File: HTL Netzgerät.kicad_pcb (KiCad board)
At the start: 2 copper layers, 140 x 65 mm, 57 parts, among them J1 0.7/20.32mm, T1 BC547, T2 BC547, T3 BC547, T4 BC547, T5 BC547, T6 BC557, T7 BC557, T8 BC639, X1 AUX1_AC1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

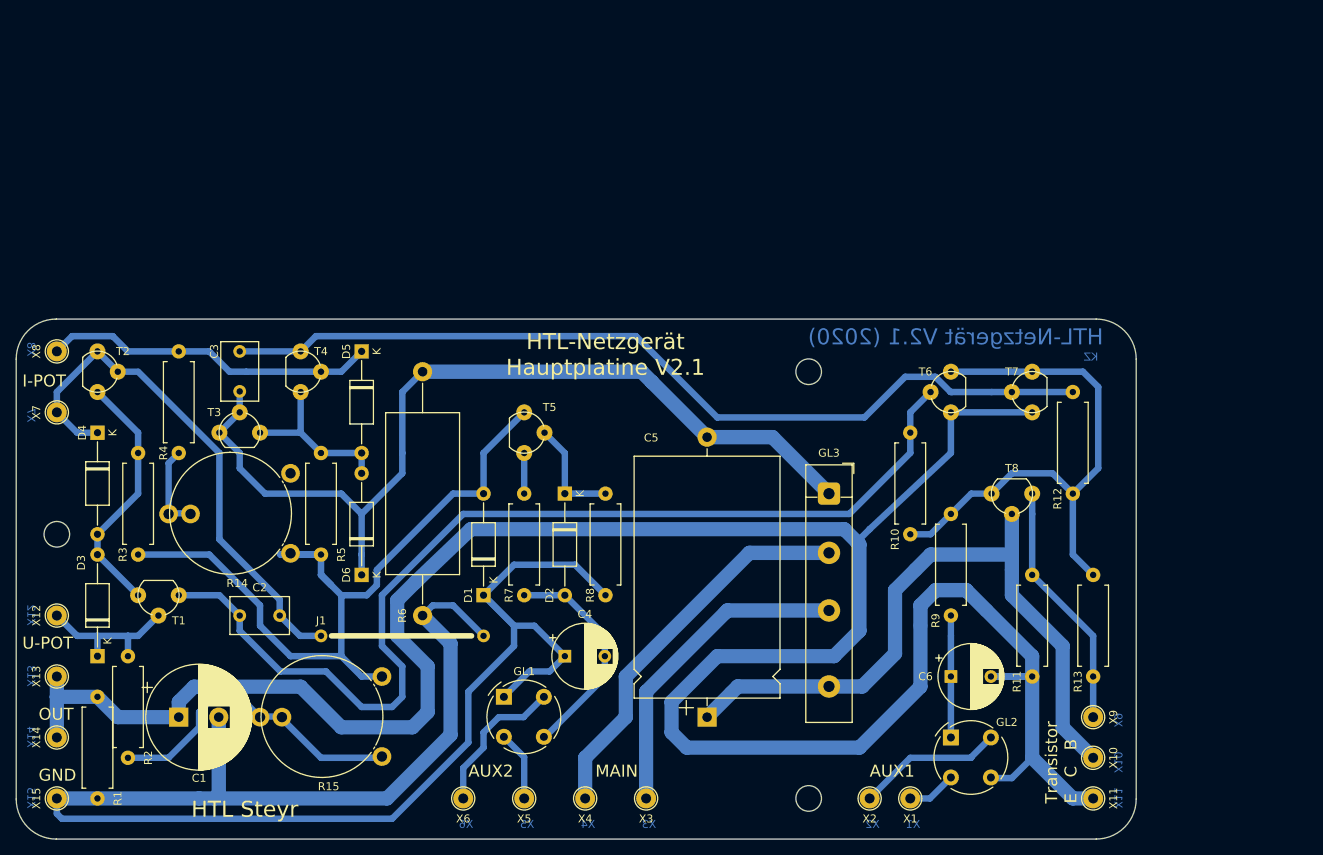
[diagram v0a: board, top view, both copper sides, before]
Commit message: v2.2 fertig, 3 Stk. bestellt (einseitig)
siehe CHANGELOG und Github Issues
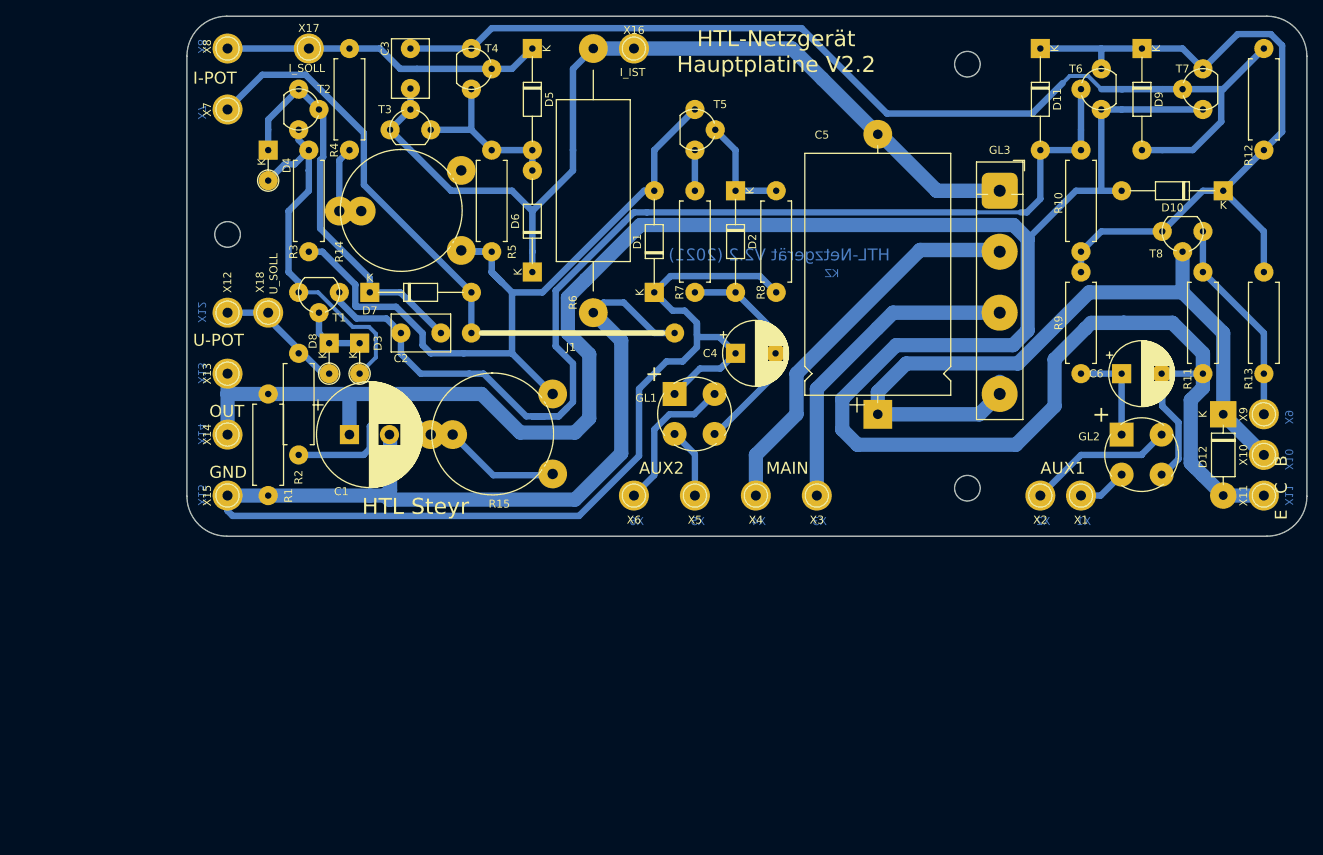
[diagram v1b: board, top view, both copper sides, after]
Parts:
- added D10: 1N4148, HTL_Netzgeraet:D_DO-35_SOD27_P12.70mm_Horizontal, F.Cu at (229.5, 56.8)
- added D11: 1N4148, HTL_Netzgeraet:D_DO-35_SOD27_P12.70mm_Horizontal, F.Cu at (206.7, 39.0)
- added D12: 1N4007, HTL_Netzgeraet:D_DO-41_SOD81_P10.16mm_Horizontal, F.Cu at (229.5, 84.8)
- added D7: 1N4148, HTL_Netzgeraet:D_DO-35_SOD27_P12.70mm_Horizontal, F.Cu at (122.9, 69.5)
- added D8: 1N4148, HTL_Netzgeraet:D_DO-35_SOD27_P3.81mm_Vertical_KathodeUp, F.Cu at (117.8, 75.9)
- added D9: 1N4148, HTL_Netzgeraet:D_DO-35_SOD27_P12.70mm_Horizontal, F.Cu at (219.4, 39.0)
- added X16: IPOT+, HTL_Netzgeraet:Einpress-Stift_Drill1.25mm, F.Cu at (155.9, 39.0)
- added X17: IPOT+, HTL_Netzgeraet:Einpress-Stift_Drill1.25mm, F.Cu at (115.2, 39.0)
- added X18: IPOT+, HTL_Netzgeraet:Einpress-Stift_Drill1.25mm, F.Cu at (110.2, 72.1)
- C2, C3: footprint Capacitor_THT:C_Rect_L7.2mm_W4.5mm_P5.00mm_FKS2_FKP2_MKS2_MKP2 -> HTL_Netzgeraet:C_Rect_L7.2mm_W4.5mm_P5.00mm_FKS2_FKP2_MKS2_MKP2
- C4, C6: footprint Capacitor_THT:CP_Radial_D8.0mm_P5.00mm -> HTL_Netzgeraet:CP_Radial_D8.0mm_P5.00mm
- C5: footprint Capacitor_THT:CP_Axial_L30.0mm_D18.0mm_P35.00mm_Horizontal -> HTL_Netzgeraet:CP_Axial_L30.0mm_D18.0mm_P35.00mm_Horizontal
- D1, D2, D5, D6: footprint Diode_THT:D_A-405_P12.70mm_Horizontal -> HTL_Netzgeraet:D_DO-35_SOD27_P12.70mm_Horizontal
- D3, D4: footprint Diode_THT:D_A-405_P12.70mm_Horizontal -> HTL_Netzgeraet:D_DO-35_SOD27_P3.81mm_Vertical_KathodeUp
- GL1, GL2: footprint Diode_THT:Diode_Bridge_Round_D9.0mm -> HTL_Netzgeraet:Diode_Bridge_Round_D9.0mm
- J1: value 0.7/20.32mm -> 0.7/25.4mm
- R6: footprint Resistor_THT:R_Axial_DIN0922_L20.0mm_D9.0mm_P30.48mm_Horizontal -> HTL_Netzgeraet:R_Axial_DIN0922_L20.0mm_D9.0mm_P30.48mm_Horizontal
- X1, X10, X11, X12, X13, X14, X15, X2, X3, X4, X5, X6, X7, X8, X9: footprint HTL_Netzgeraet:TestPoint_THTPad_D2.5mm_Drill1.25mm -> HTL_Netzgeraet:Einpress-Stift_Drill1.25mm
- moved D3 51.0 mm to (121.6, 75.9), turned to 270 degrees
- moved R12 49.1 mm to (234.6, 39.0)
- moved R6 45.7 mm to (150.8, 39.0)
- moved J1 44.8 mm to (161.0, 74.6)
- moved MK3 43.6 mm to (197.6, 94.0)
- moved GL2 43.5 mm to (216.8, 87.3)
- moved X7 43.5 mm to (105.1, 46.7)
- moved R11 43.5 mm to (227.0, 79.7)
- moved R2 43.5 mm to (114.0, 89.8)
- moved X13 43.5 mm to (105.1, 79.7)
- moved C3 43.5 mm to (127.9, 39.0)
- moved C5 43.5 mm to (186.4, 84.8)
- moved C6 43.5 mm to (216.8, 79.7)
- moved D2 43.5 mm to (168.6, 56.8)
- moved D6 43.5 mm to (143.2, 67.0)
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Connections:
- net /B_-0.6V renamed /B_-1.2V
- D3 pad 1: /V_U_FB -> Net-(D3-Pad1)
- J1 pad 2: /V_U_Ref -> Net-(D7-Pad2)
- T1 pad 2: /V_U_FB -> Net-(D3-Pad1)
- X7 pad 1: /V_U_Ref -> Net-(D7-Pad2)
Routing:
- net Net-(D7-Pad2): track 0.00 -> 52.4 mm
- net Net-(D10-Pad1): track 69.6 -> 93.2 mm
- net Net-(C3-Pad1): track 112.0 -> 132.3 mm
- net /V_U_Ref: track 66.0 -> 49.6 mm
- net /B_-1.2V: track 31.7 -> 46.7 mm
- net Net-(C2-Pad1): track 131.2 -> 142.8 mm
- net /U_OUT: track 313.6 -> 322.7 mm
- net Net-(D3-Pad1): track 0.00 -> 8.14 mm
- net /U_Main: track 85.9 -> 93.5 mm
- net Net-(R11-Pad2): track 31.1 -> 26.0 mm
- net /V_U_FB: track 19.9 -> 16.6 mm
- net /U_AUX1: track 15.2 -> 12.7 mm
- net /V_I_Ref: track 115.0 -> 117.5 mm
- net /V_I_FB: track 41.8 -> 40.2 mm
- net /-33V: track 102.2 -> 103.1 mm
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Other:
- board text added: "E C B"
- board text added: "HTL-Netzgerät Hauptplatine V2.2"
- board text added: "HTL-Netzgerät V2.2 (2021)"
- board text added: "I_IST"
- board text added: "I_SOLL"
- board text added: "U_SOLL"
- board text removed: "HTL-Netzgerät Hauptplatine V2.1"
- board text removed: "HTL-Netzgerät V2.1 (2020)"
- board text removed: "Transistor E C B"
